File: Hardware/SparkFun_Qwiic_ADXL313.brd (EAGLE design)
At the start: 25.4 x 25.4 mm, 58 parts, among them J2 QWIIC_RA, J4 QWIIC_RA, U1 ADXL313

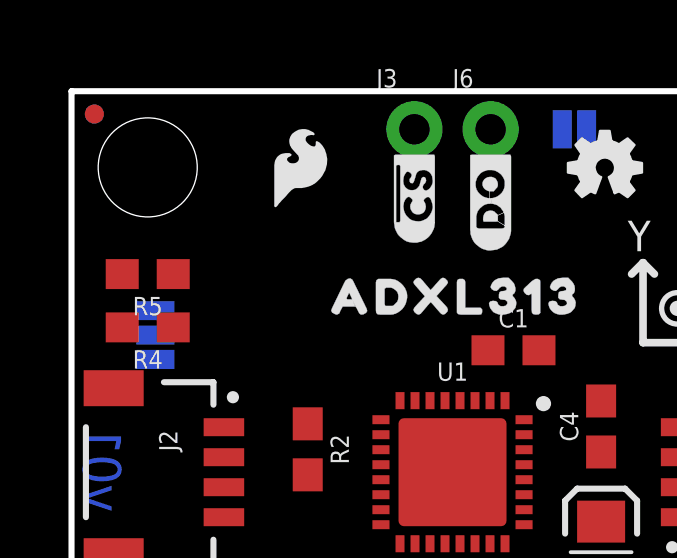
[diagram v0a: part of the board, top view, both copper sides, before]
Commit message: pullup on CS for default I2C mode (aka mode jumper)
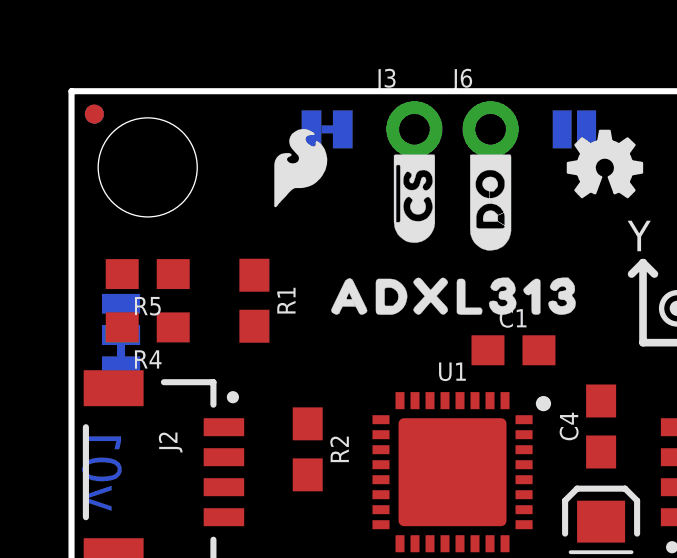
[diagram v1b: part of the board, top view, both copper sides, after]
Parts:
- removed JP7: (no value), SparkFun-Jumpers:SMT-JUMPER_3_2-NC_PASTE_SILK
- added I2C: (no value), SparkFun-Jumpers:SMT-JUMPER_3_2-NC_TRACE_SILK
- added MODE: (no value), SparkFun-Jumpers:SMT-JUMPER_2_NC_TRACE_SILK
- added R1: 10k, SparkFun-Resistors:0603
- added U$28: (no value), output:#MODE#0
- added U$29: (no value), output:OPEN#_SPI0
- added U$30: (no value), output:CLOSED#_I2C0
- moved U$27 1.14 mm to (3.30, 19.1)
- moved U$22 0.40 mm to (19.9, 22.0)
- moved U$23 0.40 mm to (18.8, 21.3)
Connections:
- new net N$3: MODE.2, R1.1
- net !CS: now also MODE.1
- net 3.3V: now also I2C.2, R1.2; no longer JP7.2
- net N$1: now also I2C.1; no longer JP7.1
- net N$2: now also I2C.3; no longer JP7.3
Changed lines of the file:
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@@
 <attribute name="VALUE" x="2.54" y="20.066" size="0.6096" layer="27" font="vector" ratio="20" rot="R180" align="top-center"/>
 </element>
-<element name="JP7" library="SparkFun-Jumpers" package="SMT-JUMPER_3_2-NC_PASTE_SILK" package3d_urn="urn:adsk.eagle:package:39294/1" value="" x="2.794" y="17.272" smashed="yes" rot="MR270">
-<attribute name="NAME" x="1.651" y="17.272" size="0.6096" layer="26" font="vector" ratio="20" rot="MR270" align="bottom-center"/>
-<attribute name="VALUE" x="3.937" y="17.272" size="0.6096" layer="28" font="vector" ratio="20" rot="MR270" align="top-center"/>
+<element name="I2C" library="SparkFun-Jumpers" package="SMT-JUMPER_3_2-NC_TRACE_SILK" package3d_urn="urn:adsk.eagle:package:39289/1" value="" x="1.651" y="17.272" smashed="yes" rot="MR270">
+<attribute name="NAME" x="0.508" y="17.272" size="0.6096" layer="26" font="vector" ratio="20" rot="MR270" align="bottom-center"/>
+<attribute name="VALUE" x="2.794" y="17.272" size="0.6096" layer="28" font="vector" ratio="20" rot="MR270" align="top-center"/>
 </element>
 <element name="J2" library="SparkFun-Connectors" package="JST04_1MM_RA" value="QWIIC_RA" x="5.08" y="12.7" smashed="yes" rot="R270">
@@
 <element name="U$20" library="output" package="#DO#ADR#0" value="" x="13.97" y="23.622" smashed="yes" rot="MR90"/>
 <element name="U$21" library="output" package="#ADR#0" value="" x="16.764" y="23.495" smashed="yes" rot="MR90"/>
-<element name="U$22" library="output" package="OPEN#_0X1D0" value="" x="20.066" y="21.59" smashed="yes" rot="MR90"/>
-<element name="U$23" library="output" package="CLOSED#_0X530" value="" x="18.923" y="20.955" smashed="yes" rot="MR90"/>
+<element name="U$22" library="output" package="OPEN#_0X1D0" value="" x="19.939" y="21.971" smashed="yes" rot="MR90"/>
+<element name="U$23" library="output" package="CLOSED#_0X530" value="" x="18.796" y="21.336" smashed="yes" rot="MR90"/>
 <element name="ADR" library="SparkFun-Jumpers" package="SMT-JUMPER_2_NO_SILK" package3d_urn="urn:adsk.eagle:package:39279/1" value="" x="16.764" y="24.13" smashed="yes" rot="MR0">
 <attribute name="NAME" x="16.764" y="25.273" size="0.6096" layer="26" font="vector" ratio="20" rot="MR0" align="bottom-center"/>
@@
 <element name="LOGO3" library="SparkFun-Aesthetics" package="SFE_LOGO_FLAME_.1" value="SFE_LOGO_FLAME.1_INCH" x="7.62" y="22.86" smashed="yes"/>
 <element name="U$19" library="output" package="ADXL3130" value="" x="12.827" y="18.542" smashed="yes"/>
-<element name="U$27" library="output" package="#I2C#0" value="" x="4.445" y="19.05" smashed="yes" rot="MR90"/>
+<element name="U$27" library="output" package="#I2C#0" value="" x="3.302" y="19.05" smashed="yes" rot="MR90"/>
+<element name="R1" library="SparkFun-Resistors" package="0603" value="10k" x="6.096" y="18.415" smashed="yes" rot="R270">
+<attribute name="NAME" x="6.858" y="18.415" size="0.6096" layer="25" font="vector" ratio="20" rot="R270" align="bottom-center"/>
+<attribute name="PROD_ID" value="RES-00824" x="6.096" y="17.145" size="1.778" layer="27" font="vector" rot="R270" display="off"/>
+<attribute name="VALUE" x="5.334" y="18.415" size="0.6096" layer="27" font="vector" ratio="20" rot="R270" align="top-center"/>
+</element>
+<element name="MODE" library="SparkFun-Jumpers" package="SMT-JUMPER_2_NC_TRACE_SILK" package3d_urn="urn:adsk.eagle:package:39281/1" value="" x="8.5217" y="24.13" smashed="yes" rot="MR0">
+<attribute name="NAME" x="8.5217" y="25.273" size="0.6096" layer="26" font="vector" ratio="20" rot="MR0" align="bottom-center"/>
+<attribute name="VALUE" x="8.5217" y="22.987" size="0.6096" layer="28" font="vector" ratio="20" rot="MR0" align="top-center"/>
+</element>
+<element name="U$28" library="output" package="#MODE#0" value="" x="8.509" y="23.622" smashed="yes" rot="MR90"/>
+<element name="U$29" library="output" package="OPEN#_SPI0" value="" x="6.477" y="22.225" smashed="yes" rot="MR90"/>
+<element name="U$30" library="output" package="CLOSED#_I2C0" value="" x="5.334" y="21.717" smashed="yes" rot="MR90"/>
 </elements>
 <signals>
 <signal name="3.3V">
-<contactref element="JP7" pad="2"/>
+<contactref element="I2C" pad="2"/>
 <contactref element="J2" pad="2"/>
 <contactref element="C4" pad="1"/>
@@
 <contactref element="JP1" pad="2"/>
 <contactref element="C1" pad="1"/>
+<contactref element="R1" pad="2"/>
 <wire x1="17.653" y1="13.374" x2="20.32" y2="12.2" width="0" layer="19" extent="1-1"/>
 <wire x1="17.653" y1="11.052" x2="17.653" y2="13.374" width="0" layer="19" extent="1-1"/>
@@
 <wire x1="7.874" y1="12.612" x2="13.95" y2="15.085" width="0" layer="19" extent="1-1"/>
 <wire x1="5.08" y1="13.2" x2="7.874" y2="12.612" width="0" layer="19" extent="1-1"/>
-<wire x1="2.794" y1="17.272" x2="5.08" y2="13.2" width="0" layer="19" extent="1-16"/>
+<wire x1="6.096" y1="17.565" x2="5.08" y2="13.2" width="0" layer="19" extent="1-1"/>
+<wire x1="1.651" y1="17.272" x2="6.096" y2="17.565" width="0" layer="19" extent="1-16"/>
 <wire x1="3.5687" y1="8.001" x2="5.08" y2="13.2" width="0" layer="19" extent="1-16"/>
 <wire x1="8.89" y1="1.27" x2="3.5687" y2="8.001" width="0" layer="19" extent="16-16"/>
@@
 <signal name="N$1">
 <contactref element="R5" pad="2"/>
-<contactref element="JP7" pad="1"/>
-<wire x1="1.69" y1="19.304" x2="2.794" y2="18.0848" width="0" layer="19" extent="1-16"/>
+<contactref element="I2C" pad="1"/>
+<wire x1="1.69" y1="19.304" x2="1.651" y2="18.3134" width="0" layer="19" extent="1-16"/>
 </signal>
 <signal name="N$2">
 <contactref element="R4" pad="2"/>
-<contactref element="JP7" pad="3"/>
-<wire x1="1.69" y1="17.526" x2="2.794" y2="16.4592" width="0" layer="19" extent="1-16"/>
+<contactref element="I2C" pad="3"/>
+<wire x1="1.69" y1="17.526" x2="1.651" y2="16.2306" width="0" layer="19" extent="1-16"/>
 </signal>
 <signal name="!CS">
 <contactref element="J3" pad="1"/>
 <contactref element="U1" pad="6"/>
+<contactref element="MODE" pad="1"/>
+<wire x1="9.0424" y1="24.13" x2="11.43" y2="24.13" width="0" layer="19" extent="16-16"/>
 <wire x1="15.085" y1="11.95" x2="11.43" y2="24.13" width="0" layer="19" extent="1-1"/>
 </signal>
@@
 <wire x1="2.5273" y1="8.001" x2="7.454" y2="8.001" width="0" layer="19" extent="1-16"/>
 </signal>
+<signal name="N$3">
+<contactref element="MODE" pad="2"/>
+<contactref element="R1" pad="1"/>
+<wire x1="6.096" y1="19.265" x2="8.001" y2="24.13" width="0" layer="19" extent="1-16"/>
+</signal>
 </signals>

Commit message: routing done
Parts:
- moved R2 1.85 mm to (7.87, 15.3)
- moved R1 0.11 mm to (6.02, 18.3)
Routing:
- net 3.3V: track 0.00 -> 55.6 mm, vias 0 -> 3
- net SCL: track 0.00 -> 47.5 mm, vias 0 -> 2
- net SDA: track 0.00 -> 46.2 mm, vias 0 -> 3
- net !CS: track 0.00 -> 30.3 mm, vias 0 -> 1
- net DO/ADR: track 0.00 -> 16.7 mm
- net INT1: track 0.00 -> 15.9 mm
- net INT2: track 0.00 -> 15.7 mm
- net N$2: track 0.00 -> 9.01 mm, vias 0 -> 1
- net N$3: track 0.00 -> 6.97 mm, vias 0 -> 1
- net N$8: track 0.00 -> 6.82 mm, vias 0 -> 1
- net N$1: track 0.00 -> 3.15 mm, vias 0 -> 1
- net GND: track 0.00 -> 2.68 mm, vias 0 -> 7
- net N$6: track 0.00 -> 1.96 mm
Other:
- board text added: "v10"
- board text removed: "v01"

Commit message: ENG checklist run changes - pre-group review
-sch cleanup
-PROD_ID for IC
-GND stiching vias and re-routed 3.3V near IC for better GND return path from filter caps
-approve DRC errors (jumper overlaps and some stubs)
-more measures
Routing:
- net 3.3V: track 55.6 -> 60.0 mm
- net !CS: track 30.3 -> 27.9 mm
- net GND: vias 7 -> 17
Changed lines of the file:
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@@
 <drawing>
 <settings>
-<setting alwaysvectorfont="yes"/>
+<setting alwaysvectorfont="no"/>
 <setting keepoldvectorfont="yes"/>
 <setting verticaltext="up"/>
@@
 <dimension x1="0" y1="25.4" x2="0" y2="0" x3="-8.89" y3="12.7" textsize="1.27" textratio="15" layer="47" unit="inch" visible="yes"/>
 <text x="15.24" y="-7.62" size="1.778" layer="51" font="vector">Pete Lewis</text>
+<dimension x1="0" y1="25.4" x2="25.4" y2="25.4" x3="12.7" y3="35.56" textsize="1.27" layer="47" unit="inch" visible="yes"/>
+<dimension x1="2.54" y1="2.54" x2="2.54" y2="22.86" x3="-3.81" y3="12.7" textsize="1.27" layer="47" unit="inch" visible="yes"/>
+<dimension x1="25.4" y1="0" x2="25.4" y2="12.7" x3="30.48" y3="6.35" textsize="1.27" layer="47" unit="inch" visible="yes"/>
+<dimension x1="0" y1="0" x2="0" y2="2.54" x3="-1.27" y3="1.27" textsize="1.27" layer="47" unit="inch" visible="yes"/>
+<dimension x1="0" y1="25.4" x2="2.54" y2="25.4" x3="1.27" y3="27.94" textsize="1.27" layer="47" unit="inch" visible="yes"/>
+<dimension x1="25.4" y1="25.4" x2="22.86" y2="25.4" x3="24.13" y3="27.94" textsize="1.27" layer="47" unit="inch" visible="yes"/>
+<dimension x1="0" y1="25.4" x2="0" y2="22.86" x3="-6.35" y3="24.13" textsize="1.27" layer="47" unit="inch" visible="yes"/>
 </plain>
 <attributes>
@@
 <element name="U1" library="adxl313" package="LFCSP" value="ADXL313" x="12.7" y="12.7" smashed="yes">
 <attribute name="NAME" x="12.7" y="15.748" size="0.6096" layer="25" font="vector" ratio="20" align="bottom-center"/>
+<attribute name="PROD_ID" value="IC-15318" x="12.7" y="12.7" size="1.778" layer="27" display="off"/>
 <attribute name="VALUE" x="12.7" y="9.652" size="0.6096" layer="27" font="vector" ratio="20" align="top-center"/>
 </element>
@@
 <contactref element="C1" pad="1"/>
 <contactref element="R1" pad="2"/>
-<wire x1="20.32" y1="12.2" x2="17.653" y2="12.2" width="0.508" layer="1"/>
+<wire x1="20.32" y1="12.2" x2="18.542" y2="12.2" width="0.508" layer="1"/>
+<wire x1="18.542" y1="12.2" x2="17.653" y2="12.2" width="0.508" layer="1"/>
 <wire x1="17.653" y1="12.2" x2="16.502" y2="12.2" width="0.508" layer="1"/>
 <wire x1="16.502" y1="12.2" x2="16.256" y2="12.446" width="0.508" layer="1"/>
@@
 <wire x1="13.95" y1="15.748" x2="13.95" y2="16.696" width="0.254" layer="1"/>
 <wire x1="13.95" y1="16.696" x2="13.882" y2="16.764" width="0.254" layer="1"/>
-<wire x1="16.256" y1="12.446" x2="16.256" y2="12.954" width="0.254" layer="1"/>
-<wire x1="16.256" y1="12.954" x2="16.8402" y2="13.5382" width="0.254" layer="1"/>
-<wire x1="16.8402" y1="13.5382" x2="16.8402" y2="14.7828" width="0.254" layer="1"/>
-<wire x1="16.8402" y1="14.7828" x2="15.875" y2="15.748" width="0.254" layer="1"/>
-<wire x1="15.875" y1="15.748" x2="13.95" y2="15.748" width="0.254" layer="1"/>
 <wire x1="8.89" y1="1.27" x2="8.89" y2="8.001" width="0.508" layer="16"/>
 <via x="8.9154" y="13.208" extent="1-16" drill="0.381"/>
@@
 <wire x1="6.0198" y1="15.3416" x2="6.0198" y2="16.3322" width="0.254" layer="1"/>
 <wire x1="6.8952" y1="14.4662" x2="6.0198" y2="15.3416" width="0.254" layer="1"/>
+<wire x1="13.882" y1="16.764" x2="13.882" y2="17.4634" width="0.254" layer="1"/>
+<wire x1="13.882" y1="17.4634" x2="14.1224" y2="17.7038" width="0.254" layer="1"/>
+<wire x1="14.1224" y1="17.7038" x2="17.4487375" y2="17.7038" width="0.254" layer="1"/>
+<wire x1="18.542" y1="16.6105375" x2="18.542" y2="12.2" width="0.254" layer="1"/>
+<wire x1="17.4487375" y1="17.7038" x2="18.542" y2="16.6105375" width="0.254" layer="1"/>
 </signal>
 <signal name="GND">
@@
 <via x="5.1054" y="15.1892" extent="1-16" drill="0.381"/>
 <via x="21.6154" y="11.1252" extent="1-16" drill="0.381"/>
-<via x="16.0528" y="13.97" extent="1-16" drill="0.381"/>
-<via x="17.6022" y="16.2814" extent="1-16" drill="0.381"/>
+<via x="16.5608" y="13.97" extent="1-16" drill="0.381"/>
+<via x="17.272" y="16.637" extent="1-16" drill="0.381"/>
 <via x="19.1008" y="8.255" extent="1-16" drill="0.381"/>
 <wire x1="15.085" y1="13.45" x2="15.8376" y2="13.45" width="0.254" layer="1"/>
@@
 <wire x1="14.45" y1="14.45" x2="14.1986" y2="14.1986" width="0.254" layer="1"/>
 <via x="15.2654" y="3.0734" extent="1-16" drill="0.381"/>
+<via x="12.7" y="3.2004" extent="1-16" drill="0.381"/>
+<via x="10.1346" y="6.1976" extent="1-16" drill="0.381"/>
+<via x="7.239" y="9.1186" extent="1-16" drill="0.381"/>
+<via x="17.8054" y="4.1402" extent="1-16" drill="0.381"/>
+<via x="14.9606" y="6.9342" extent="1-16" drill="0.381"/>
+<via x="10.9728" y="19.7612" extent="1-16" drill="0.381"/>
+<via x="12.7508" y="21.4122" extent="1-16" drill="0.381"/>
+<via x="9.8552" y="21.4122" extent="1-16" drill="0.381"/>
+<via x="7.6708" y="17.5514" extent="1-16" drill="0.381"/>
+<via x="16.3068" y="15.4432" extent="1-16" drill="0.381"/>
 </signal>
 <signal name="SCL">
@@
 <wire x1="16.0274" y1="11.6586" x2="16.0274" y2="7.9756" width="0.254" layer="1"/>
 <via x="16.0274" y="7.9756" extent="1-16" drill="0.381"/>
-<wire x1="16.0274" y1="7.9756" x2="16.5862" y2="7.9756" width="0.254" layer="16"/>
-<wire x1="20.2692" y1="11.6586" x2="16.5862" y2="7.9756" width="0.254" layer="16"/>
-<wire x1="20.2692" y1="11.6586" x2="20.2692" y2="17.5006" width="0.254" layer="16"/>
-<wire x1="20.2692" y1="17.5006" x2="17.2974" y2="20.4724" width="0.254" layer="16"/>
-<wire x1="15.0876" y1="20.4724" x2="11.43" y2="24.13" width="0.254" layer="16"/>
+<wire x1="19.3548" y1="11.303" x2="16.0274" y2="7.9756" width="0.254" layer="16"/>
+<wire x1="19.3548" y1="11.303" x2="19.3548" y2="16.2052" width="0.254" layer="16"/>
+<wire x1="19.3548" y1="16.2052" x2="11.43" y2="24.13" width="0.254" layer="16"/>
 <wire x1="15.736" y1="11.95" x2="16.0274" y2="11.6586" width="0.254" layer="1"/>
-<wire x1="17.2974" y1="20.4724" x2="15.0876" y2="20.4724" width="0.254" layer="16"/>
 <wire x1="11.43" y1="24.13" x2="9.0424" y2="24.13" width="0.254" layer="16"/>
 </signal>
@@
 <mfgpreviewcolor name="substratecolor" color="0xFF786E46"/>
 </mfgpreviewcolors>
+<errors>
+</errors>
 </board>
 </drawing>

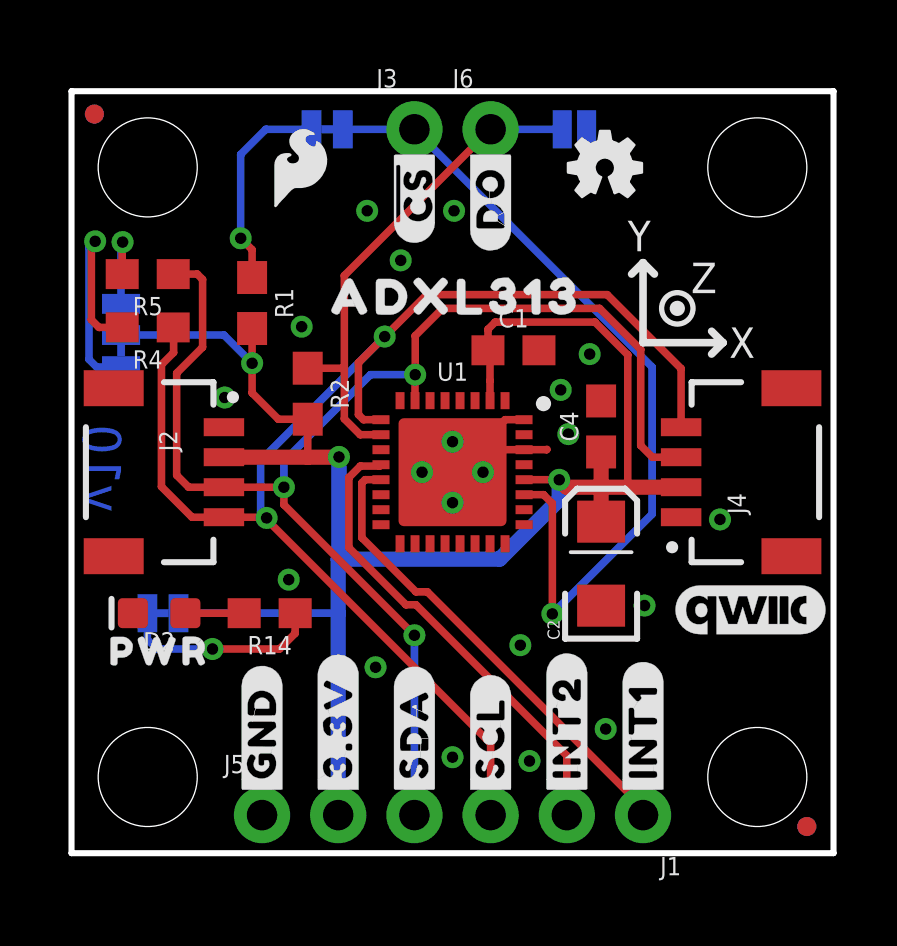
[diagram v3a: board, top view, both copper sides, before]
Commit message: Group Review changes
-Removed MODE Jumper, CS should always be tied high.
-Added optional Resistor on power input to IC, for potential RC filter.
-SDA/SCL corrected
- corrected pin location in device footprint. (they were mirrored)
- 3 vias under IC are now actually named GND
- CS and SDO were swapped with INTs so all data lines are on the same row of headers
- End caps on buzzards corrected.
- Moved to all I2C labels on top and SPI labels on bottom.
- added tRestrict near pads on IC to stop gdn flow on top corner and natural jumper of two inner GND pads.
- Symbol now has NC pin and Reserved pin
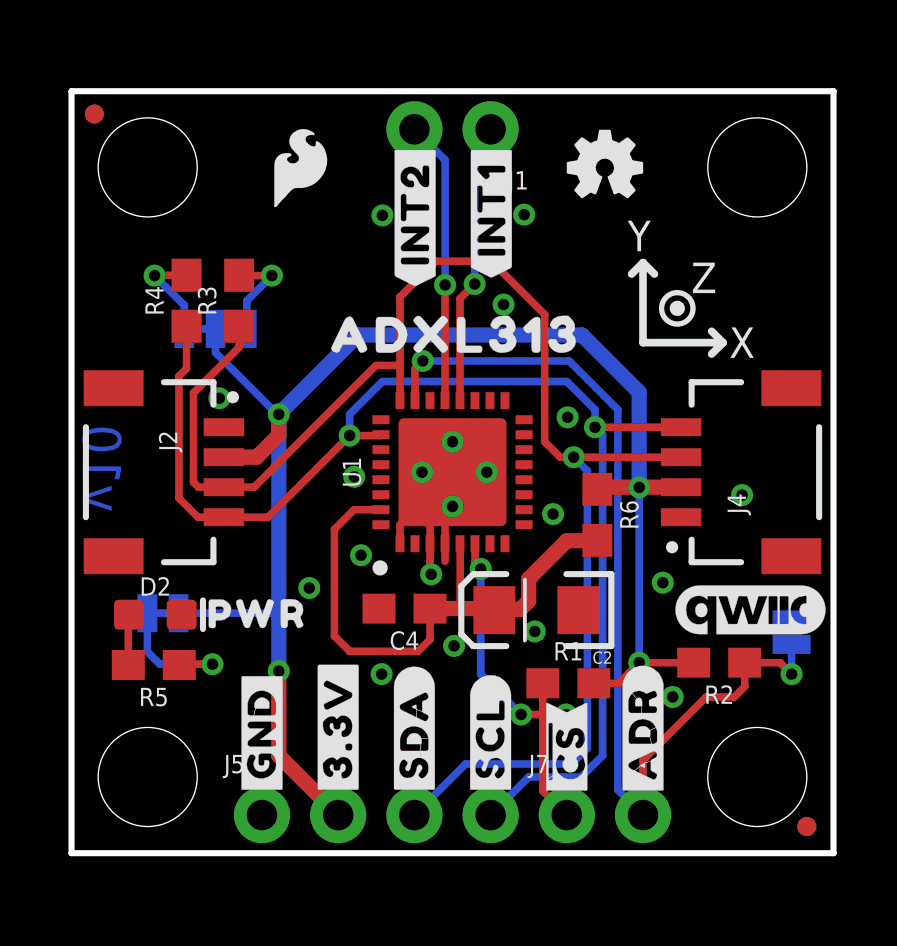
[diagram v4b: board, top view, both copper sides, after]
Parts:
- removed C1: 0.1uF, SparkFun-Capacitors:0603
- removed J3, J6: (no value), SparkFun-Connectors:1X01_NO_SILK
- removed MODE: (no value), SparkFun-Jumpers:SMT-JUMPER_2_NC_TRACE_SILK
- removed R14: 1k, SparkFun-Resistors:0603
- removed U$12: (no value), output:#SCL#0
- removed U$26: (no value), output:#DO#0
- removed U$29: (no value), output:OPEN#_SPI0
- added J7: (no value), SparkFun-Connectors:1X02_NO_SILK
- added R3: 4.7k, SparkFun-Resistors:0603
- added R6: 0, SparkFun-Resistors:0603
- R5: value 4.7k -> 1k
- U$10: device output:#SDA#0 -> output:#SDI#0
- U$20: device output:#DO#ADR#0 -> output:#SCLK#0
- U$28: device output:#MODE#0 -> output:#ADR#0
- U$30: device output:CLOSED#_I2C0 -> output:#SDO#0
- moved U$28 24.3 mm to (19.1, 1.75), flipped to the top
- moved U$30 24.2 mm to (19.1, 1.75)
- moved J1 23.4 mm to (14.0, 24.1)
- moved U$13 22.6 mm to (11.5, 23.8)
- moved U$14 22.6 mm to (11.5, 23.8)
- moved U$15 22.6 mm to (14.0, 23.8)
- moved U$16 22.6 mm to (14.0, 23.8)
- moved U$17 22.5 mm to (16.5, 1.75)
- moved U$18 22.5 mm to (16.5, 1.75)
- moved U$20 21.9 mm to (13.9, 1.70)
- moved ADR 18.3 mm to (24.0, 7.37), turned to 270 degrees
- moved U$21 17.0 mm to (24.0, 8.13)
- moved R1 16.5 mm to (16.6, 5.66), turned to 0 degrees
- moved R2 16.4 mm to (21.6, 6.35), turned to 180 degrees
- moved R5 13.0 mm to (2.74, 6.27)
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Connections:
- removed net DO/ADR: ADR.2, J6.1, R2.1, U1.23
- new net SDO/ADR: ADR.2, J7.2, R2.1, U1.23
- net !CS: now also J7.1, R1.1; no longer J3.1, MODE.1
- net 3.3V: now also R6.1; no longer C1.1, C2.A, C4.1, U1.31, U1.5
- net GND: no longer C1.2
- net N$1: now also R3.2; no longer R5.2
- net N$3: now also C2.A, C4.1, R6.2, U1.31, U1.5; no longer MODE.2, R1.1
- net N$6: now also R5.2; no longer R14.2
- net N$8: now also R5.1; no longer R14.1
- net SCL: now also U1.26; no longer U1.24
- net SDA: now also R3.1, U1.24; no longer R5.1, U1.26
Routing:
- net SDO/ADR: track 0.00 -> 32.2 mm, vias 0 -> 2
- net DO/ADR: track 16.7 -> 0.00 mm
- net !CS: track 27.9 -> 11.8 mm, vias 1 -> 2
- net N$3: track 6.97 -> 19.1 mm, vias 1 -> 0
- net 3.3V: track 60.0 -> 53.5 mm, vias 3 -> 4
- net INT1: track 15.9 -> 9.47 mm, vias 0 -> 1
- net INT2: track 15.7 -> 9.47 mm, vias 0 -> 1
- net N$2: track 9.01 -> 3.26 mm
- net SCL: track 47.5 -> 42.8 mm
- net SDA: track 46.2 -> 49.6 mm, vias 3 -> 1
- net N$8: track 6.82 -> 4.74 mm
- net GND: track 2.68 -> 4.59 mm, vias 17 -> 21
